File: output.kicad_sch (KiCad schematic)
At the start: 2 parts, among them J1 Conn_01x02

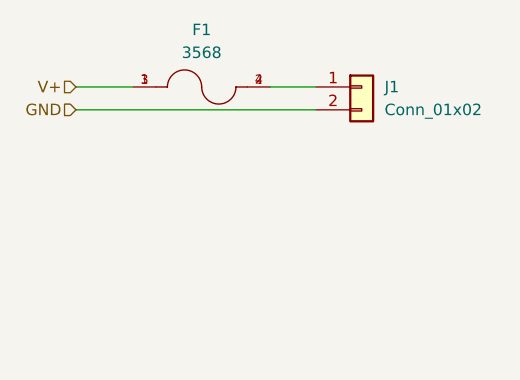
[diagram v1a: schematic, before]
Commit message: added TVS diodes and routed traces
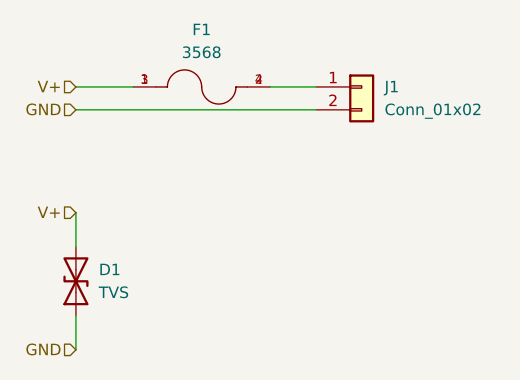
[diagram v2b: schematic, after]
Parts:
- added D1: TVS, Diode_SMD:D_0603_1608Metric, symbol Device:D_TVS
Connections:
- net GND: now also D1.1 (A1)
- net V+: now also D1.2 (A2)
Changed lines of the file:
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@@
+	(wire
+		(pts
+			(xy 38.1 50.8) (xy 38.1 54.61)
+		)
+		(stroke
+			(width 0)
+			(type default)
+		)
+	)
 	(wire
 		(pts
@@
 			(width 0)
 			(type default)
+		)
+	)
+	(wire
+		(pts
+			(xy 38.1 62.23) (xy 38.1 66.04)
+		)
+		(stroke
+			(width 0)
+			(type default)
+		)
+	)
+	(hierarchical_label "V+"
+		(shape input)
+		(at 38.1 50.8 180)
+		(effects
+			(font
+				(size 1.27 1.27)
+			)
+			(justify right)
+		)
+	)
+	(hierarchical_label "GND"
+		(shape input)
+		(at 38.1 66.04 180)
+		(effects
+			(font
+				(size 1.27 1.27)
+			)
+			(justify right)
 		)
 	)
@@
 					(unit 1)
 				)
+			)
+		)
+	)
+	(symbol
+		(lib_id "Device:D_TVS")
+		(at 38.1 58.42 90)
+		(unit 1)
+		(exclude_from_sim no)
+		(in_bom yes)
+		(on_board yes)
+		(dnp no)
+		(fields_autoplaced yes)
+		(property "Reference" "D1"
+			(at 40.64 57.1499 90)
+			(effects
+				(font
+					(size 1.27 1.27)
+				)
+				(justify right)
+			)
+		)
+		(property "Value" "TVS"
+			(at 40.64 59.6899 90)
+			(effects
+				(font
+					(size 1.27 1.27)
+				)
+				(justify right)
+			)
+		)
+		(property "Footprint" "Diode_SMD:D_0603_1608Metric"
+			(at 38.1 58.42 0)
+			(effects
+				(font
+					(size 1.27 1.27)
+				)
+				(hide yes)
+			)
+		)
+		(property "Datasheet" "~"
+			(at 38.1 58.42 0)
+			(effects
+				(font
+					(size 1.27 1.27)
+				)
+				(hide yes)
+			)
+		)
+		(property "Description" "Bidirectional transient-voltage-suppression diode"
+			(at 38.1 58.42 0)
+			(effects
+				(font
+					(size 1.27 1.27)
+				)
+				(hide yes)
+			)
+		)
+		(property "P/N" "CPDUC5V0R-HF "
+			(at 38.1 58.42 0)
+			(effects
+				(font
+					(size 1.27 1.27)
+				)
+				(hide yes)
+			)
+		)
+		(pin "1"
+		)
+		(pin "2"
+		)
+		(instances
+			(project "PS-LVDistributionPCB"
+				(path "/bae4e46c-28ae-4193-a5e0-928c081802f5/0c5dc2b3-5678-4805-b517-2383e282d677"
+					(reference "D11")
+					(unit 1)
+				)
+				(path "/bae4e46c-28ae-4193-a5e0-928c081802f5/18ac63a7-3bca-4c43-b27b-65a05d7d7b87"
+					(reference "D3")
+					(unit 1)
+				)
+				(path "/bae4e46c-28ae-4193-a5e0-928c081802f5/2368929e-74fb-45db-9707-57b7d5bb9582"
+					(reference "D6")
+					(unit 1)
+				)
+				(path "/bae4e46c-28ae-4193-a5e0-928c081802f5/2816337e-2e2f-49b6-8e14-8a47d5a2a9d1"
+					(reference "D8")
+					(unit 1)
+				)
+				(path "/bae4e46c-28ae-4193-a5e0-928c081802f5/59c10fe7-a3ff-4c09-b5ab-17cf92d08f6c"
+					(reference "D10")
+					(unit 1)
+				)
+				(path "/bae4e46c-28ae-4193-a5e0-928c081802f5/5c3564df-81ec-4394-b500-8c1eff5644b2"
+					(reference "D2")
+					(unit 1)
+				)
+				(path "/bae4e46c-28ae-4193-a5e0-928c081802f5/68f2420e-006e-47d2-9129-3e87fca9ad04"
+					(reference "D4")
+					(unit 1)
+				)
+				(path "/bae4e46c-28ae-4193-a5e0-928c081802f5/8bcb5444-63d3-40d8-951f-42e39a0c9384"
+					(reference "D5")
+					(unit 1)
+				)
+				(path "/bae4e46c-28ae-4193-a5e0-928c081802f5/a1849b17-8bf2-4c90-964d-3f4d88c7d452"
+					(reference "D1")
+					(unit 1)
+				)
+				(path "/bae4e46c-28ae-4193-a5e0-928c081802f5/ce1e68f1-cba2-4e41-af5d-2c6f5daea4ec"
+					(reference "D9")
+					(unit 1)
+				)
+				(path "/bae4e46c-28ae-4193-a5e0-928c081802f5/e3c5a549-d3db-4a69-870b-863cbd46f0ad"
+					(reference "D7")
+					(unit 1)
+				)
+				(path "/bae4e46c-28ae-4193-a5e0-928c081802f5/eaa12baa-4d75-41da-8f13-104e26b06c51"
+					(reference "D12")
+					(unit 1)
+				)
